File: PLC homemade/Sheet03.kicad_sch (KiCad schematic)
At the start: 0 parts

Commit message: :spanner:atarted on rs485 interface and ADC
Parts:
- added C21, C22, C23, C24: 10p, symbol Device:C
- added C25: 100nF 50V, symbol Device:C
- added D4, D5, D6, D7: BAT54S, Package_TO_SOT_SMD:SOT-23, symbol Diode:BAT54S
- added R23, R25: 5.1K, symbol Device:R
- added R24, R26, R27, R28, R31: 10K, symbol Device:R
- added R30, R32: 150R, symbol Device:R
- added U4: LM324ADT, LM324ADT:SOIC127P600X175-14N, symbol LM324ADT:LM324ADT
- added U5: SN74LVC1G125DRL, Package_TO_SOT_SMD:Texas_R-PDSO-N5_DRL-5, symbol 74xGxx:SN74LVC1G125DRL
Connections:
- new net +12V_ADC: U4.4 (VCC+)
- new net 3V3: C25.2, D4.1 (A), D5.1 (A), D6.1 (A), D7.1 (A), U5.5 (VCC)
- new net 485RX: U5.4
- new net 485RX13: R27.2, U5.2
- new net AGND: C21.2, C22.2, C23.2, C24.2, C25.1, D4.3 (COM), D5.3 (COM), D6.3 (COM), D7.3 (COM), R24.2, R26.2, R30.2, R32.2, U4.11 (VCC-), U5.1, U5.3 (GND)
- new net CHN_1: R23.1
- new net CHN_2: R25.1
- new net CHN_3: R28.1, R30.1
- new net CHN_4: R31.1, R32.1
- new net INA1: D7.2 (K), U4.1 (OUT1), U4.3 (POS_1)
- new net INA2: D6.2 (K), U4.5 (POS_2), U4.7 (OUT2)
- new net INA3: D5.2 (K), U4.10 (POS_3), U4.8 (OUT3)
- new net INA4: D4.2 (K), U4.12 (POS_4), U4.14 (OUT4)
- new net INPUT_AA0: C21.1, R23.2, R24.1
- new net INPUT_AA1: C22.1, R25.2, R26.1
- new net INPUT_AA2: C23.1, R28.2
- new net INPUT_AA3: C24.1, R31.2
- new net VCC: R27.1
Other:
- note added: "0-5V"
- note added: "4_20MA"

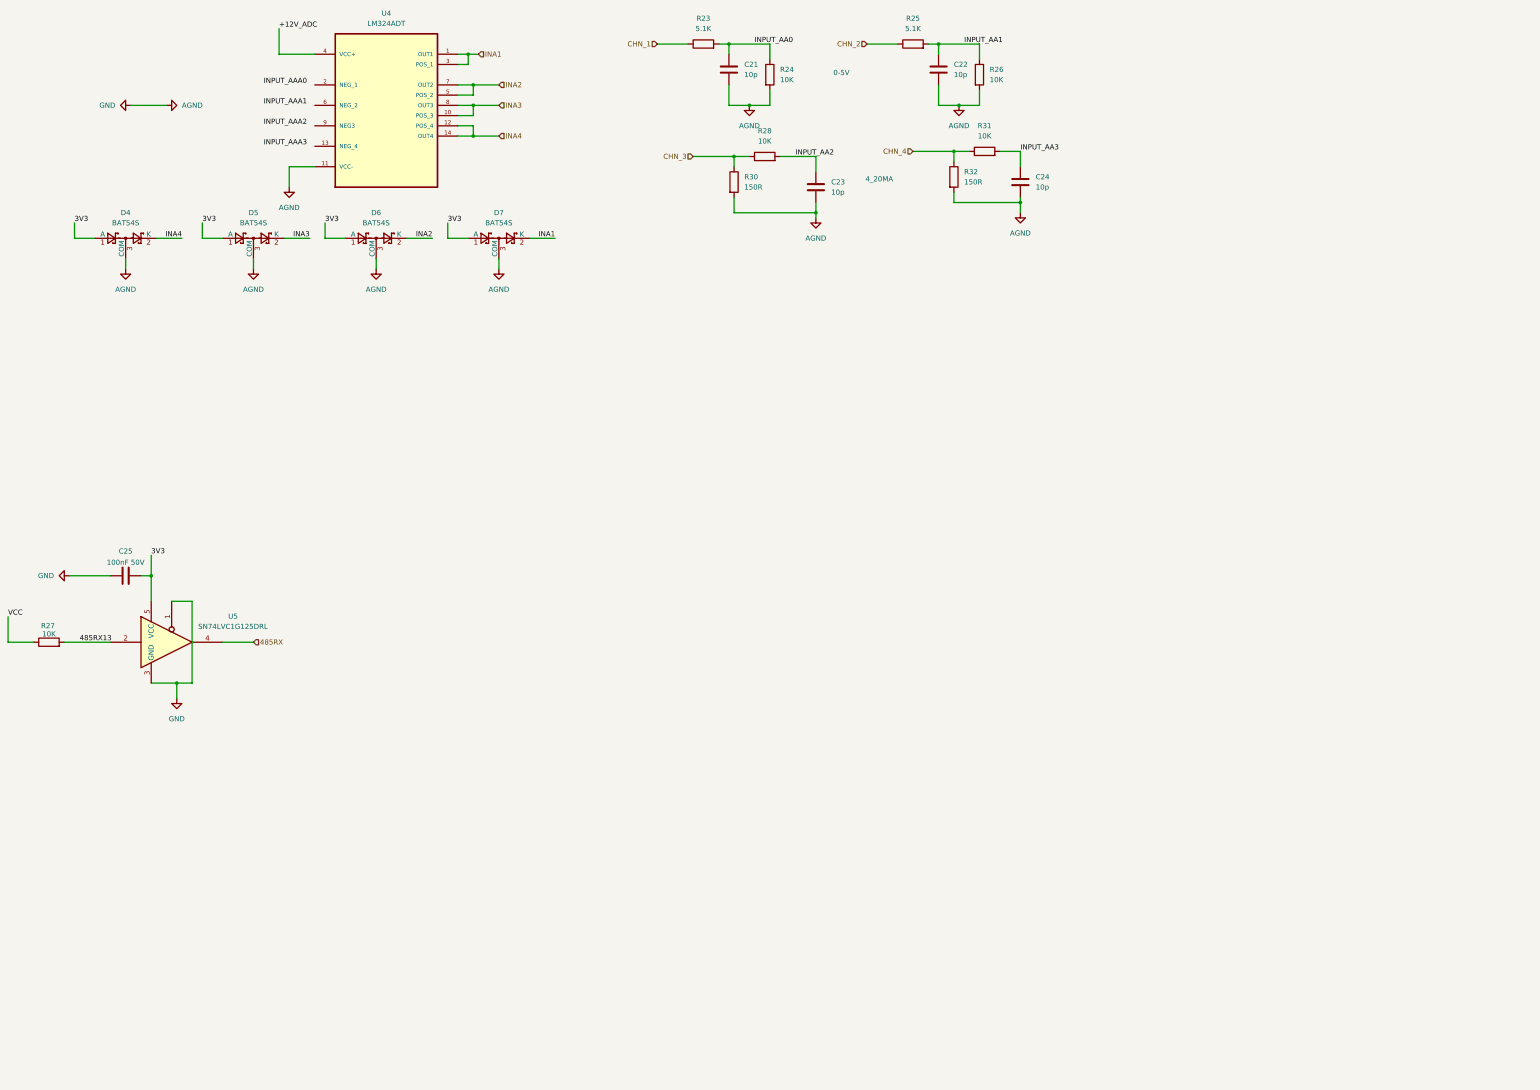
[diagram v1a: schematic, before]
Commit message: :zap: completing basics of rs485
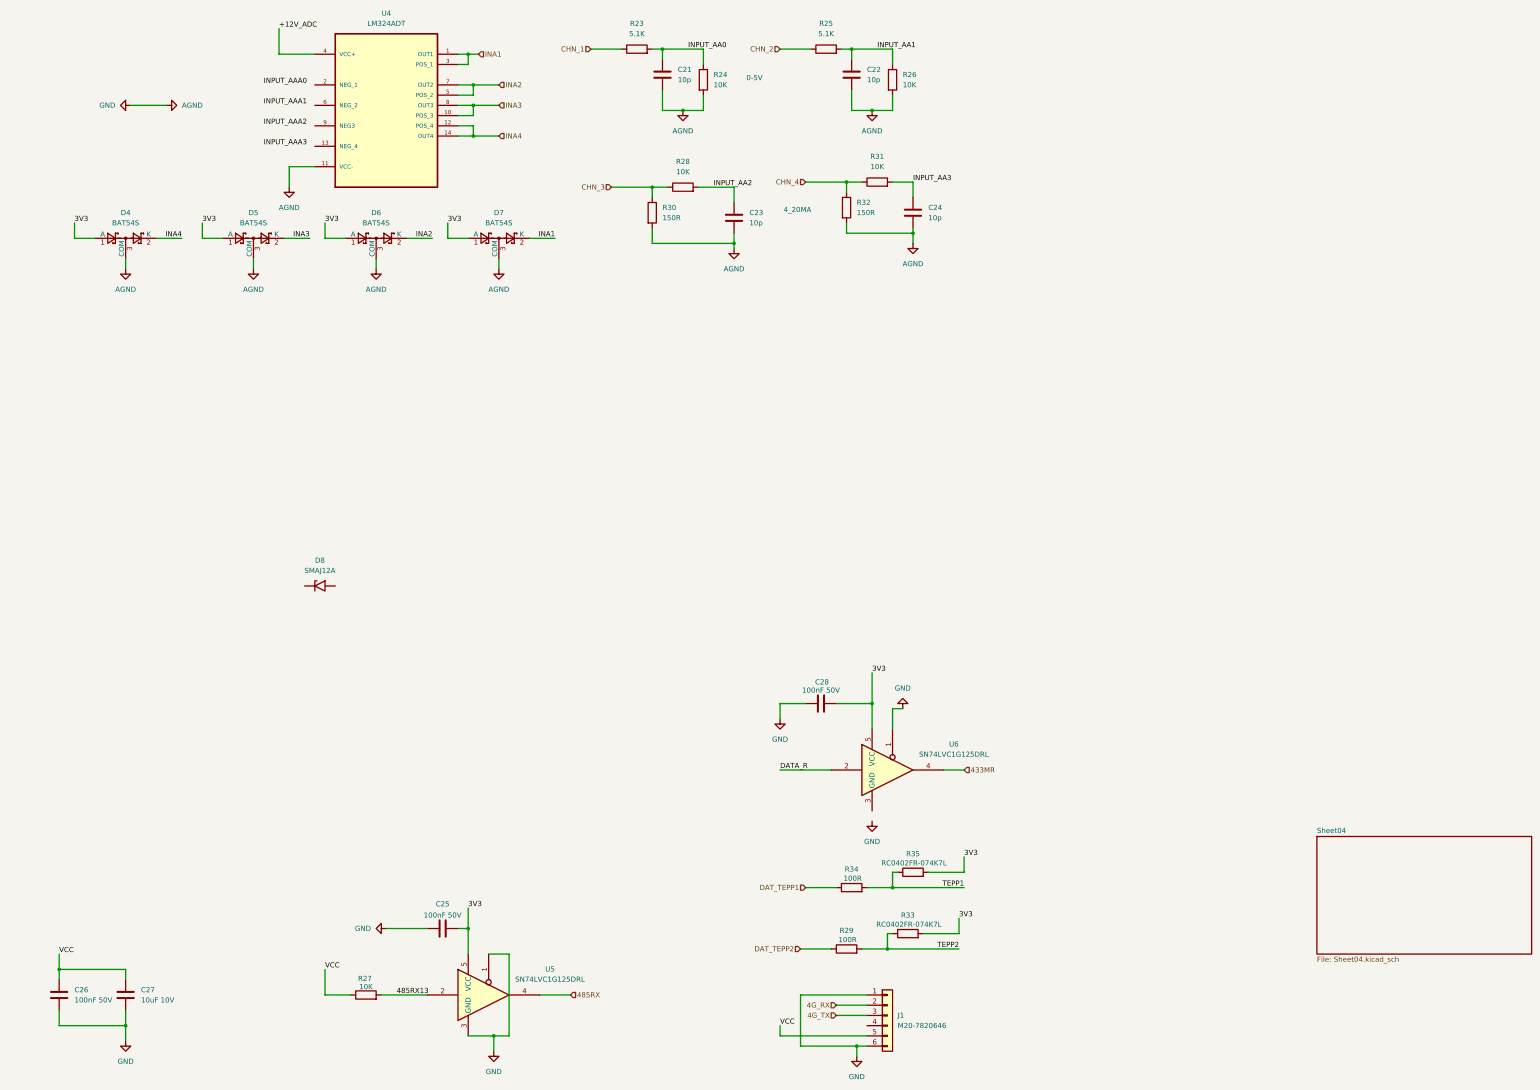
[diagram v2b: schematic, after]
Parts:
- added C26, C28: 100nF 50V, symbol Device:C
- added C27: 10uF 10V, symbol Device:C
- added D8: SMAJ12A, Diode_SMD:D_SMA, symbol Diode:SMAJ12A
- added J1: M20-7820646, symbol Connector_Generic:Conn_01x06
- added R29, R34: 100R, symbol Device:R
- added R33, R35: RC0402FR-074K7L, symbol Device:R
- added U6: SN74LVC1G125DRL, Package_TO_SOT_SMD:Texas_R-PDSO-N5_DRL-5, symbol 74xGxx:SN74LVC1G125DRL
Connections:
- net 3V3: now also C28.2, R33.2, R35.2, U6.5 (VCC)
- net AGND: now also C26.2, C27.2, C28.1, J1.1 (Pin_1), J1.6 (Pin_6), U6.1
- net VCC: now also C26.1, C27.1, J1.5 (Pin_5)
- new net 433MR: U6.4
- new net 4G_RX: J1.2 (Pin_2)
- new net 4G_TX: J1.3 (Pin_3)
- new net DATA_R: U6.2
- new net DAT_TEPP1: R34.1
- new net DAT_TEPP2: R29.1
- new net TEPP1: R34.2, R35.1
- new net TEPP2: R29.2, R33.1
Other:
- added sheet Sheet04 (Sheet04.kicad_sch)
- moved on the sheet: C21, C22, C23, C24, C25, R23, R24, R25, R26, R27, R28, R30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

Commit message: :green_heart: CoRRECTED pOWER eRRORS
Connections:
- net INPUT_AAA0: now also U4.2 (NEG_1)
- net INPUT_AAA1: now also U4.6 (NEG_2)
- net INPUT_AAA2: now also U4.9 (NEG3)
- net INPUT_AAA3: now also U4.13 (NEG_4)
- net 3V3 renamed 3.3V

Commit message: :art: COMPLETED SHEET3
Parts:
- removed D8: SMAJ12A, Diode_SMD:D_SMA, symbol Diode:SMAJ12A
- added C41, C44, C47: 1uF 16V, symbol Device:C
- added C42, C43, C45, C46, C48: 100nF 50V, symbol Device:C
- added D11: SR70-02CTG, SR70-02CTG:SOT-143-4_L2.9-W1.3-P1.92-LS2.4-BL, symbol SR70-02CTG:SR70-02CTG
- added D12, D13: SMAJ12A, Diode_SMD:D_SMA, symbol Diode:SMAJ12A
- added F1, F2: MF-MSMF010-2, MF-MSMF010-2:FUSER_MF-MSMF010-2, symbol MF-MSMF010-2:MF-MSMF010-2
- added L2, L3: 500mA 600R, symbol Device:L
- added R65, R67, R68: 4K7, symbol Device:R
- added R66: 120R, symbol Device:R
- added U11: GP8403-TC50-EW_C3152007, GP8403-TC50-EW:ESSOP-10_L4.9-W3.9-P1.00-LS6.0-BL-EP, symbol GP8403-TC50-EW:GP8403-TC50-EW_C3152007
- added U12: MAX13487EESAT, MAX13487EESAT:SOIC127P600X175-8N, symbol MAX13487EESAT:MAX13487EESAT
- added U13, U14: SMBJ7.0CA-Q, SMBJ7:SMB_L4.3-W3.6-LS5.4-BI, symbol SMBJ7.0CA-Q:SMBJ7.0CA-Q
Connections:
- net +12V_ADC: now also C47.1, C48.1, L3.2
- net 485RX13: now also U12.1 (RO)
- net AGND: now also C41.2, C42.2, C43.2, C44.2, C45.2, C46.2, C47.2, C48.2, D11.1 (GND), D12.2 (A2), D13.2 (A2), U11.11 (EP), U11.3 (A0), U11.4 (A1), U11.6 (GND), U11.9 (A2), U13.2 (A), U14.2 (A)
- net VCC: now also R65.1
- new net: F1.1, R66.2, R68.2, U12.7 (B)
- new net: R65.2, U12.2 (~{RE}), U12.3 (~{SHDN})
- new net: R68.1, U12.5 (GND)
- new net: R66.1, U12.6 (A)
- new net: R67.1, U12.8 (VCC)
- new net: C44.1, U11.10 (V5V)
- new net: F2.1, R67.2
- new net 12V: L2.1, L3.1
- new net 485TX: U12.4 (DI)
- new net A1/RX1: F2.2, U13.1 (K)
- new net B1/TX1: F1.2, U14.1 (K)
- new net DAC0: C46.1, D11.3 (IO2), D13.1 (A1), U11.8 (VOUT0)
- new net DAC1: C45.1, D11.2 (IO1), D12.1 (A1), U11.7 (VOUT1)
- new net IIC_SCL: U11.1 (SCLK)
- new net II_SDA: U11.2 (SDA)
- new net VCC_DAC: C41.1, C42.1, C43.1, D11.4 (VCC), L2.2, U11.5 (VCC)
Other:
- note added: "2CH 0-10V OUT"
- note added: "4G_PS INTERFACE"
- note added: "ADC"
- note added: "RS485"
- moved on the sheet: C21, C22, C23, C24, D4, D5, D6, D7, R23, R24, R25, R26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

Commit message: :tada: Added small changes
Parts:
- added J16: Conn_01x04, symbol Connector_Generic:Conn_01x04
- added J17: Conn_01x02, symbol Connector_Generic:Conn_01x02
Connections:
- net CHN_1: now also J16.1 (Pin_1)
- net CHN_2: now also J16.2 (Pin_2)
- net CHN_3: now also J16.3 (Pin_3)
- net CHN_4: now also J16.4 (Pin_4)
- net DAC0: now also J17.1 (Pin_1)
- net DAC1: now also J17.2 (Pin_2)
